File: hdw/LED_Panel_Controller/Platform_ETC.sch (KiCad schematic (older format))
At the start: 7 parts

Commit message: lots of schematic progress
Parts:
- U?: Configuration (none) -> ETC
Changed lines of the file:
@@
 encoding utf-8
 Sheet 14 34
-Title "Pulse Oximeter"
-Date "2020-08-01"
+Title "LED Panel Controller"
+Date "2020-12-23"
 Rev "A"
-Comp "Drew Maatman"
+Comp "Drew Maatman, Logan Wedel"
 Comment1 ""
 Comment2 ""
@@
 F 3 "https://datasheets.maximintegrated.com/en/ds/DS1683.pdf" H 4740 4400 60  0001 C CNN
 F 4 "DS1683S+-ND" H 4940 3850 60  0001 C CNN "Digi-Key PN"
+F 5 "ETC" H 4840 3640 50  0000 C CNN "Configuration"
 	1    4840 4100
 	1    0    0    -1

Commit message: made a lot more schematic progress
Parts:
- removed C? (x2): 10uF, Capacitors_SMD:C_0402, symbol Custom_Library:C_Custom
- added C? (x2): 10uF, Capacitors_SMD:C_0402, symbol Custom_Library:C_Custom
- C? (x2), D?: Configuration (none) -> ETC
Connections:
- net GND: now also C?.2, C?.2
- net at C?.1, C?.1, D?.1 (K)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: now also C?.1, C?.1
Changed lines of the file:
@@
 F 3 "www.st.com/resource/en/datasheet/bat48.pdf" H 2880 2660 50  0001 C CNN
 F 4 "497-5711-1-ND" H 2880 2660 50  0001 C CNN "Digi-Key PN"
+F 5 "ETC" V 2880 2830 50  0000 C CNN "Configuration"
 	1    2880 2660
 	0    -1   -1   0
@@
 F 6 "X5R" H 2730 3020 50  0000 R CNN "Dielectric"
 F 7 "490-13211-1-ND" H 2880 3120 50  0001 C CNN "Digi-Key PN"
+F 8 "ETC" H 2730 3300 50  0000 R CNN "Configuration"
 	1    2880 3120
-	1    0    0    -1
-$EndComp
-$Comp
-L Custom_Library:C_Custom C?
-U 1 1 5EC1781D
-P 3530 3120
-AR Path="/5CB7718D/5EC1781D" Ref="C?"  Part="1"
-AR Path="/5E0DC082/5EC1781D" Ref="C?"  Part="1"
-AR Path="/5E0F9110/5EC1781D" Ref="C?"  Part="1"
-AR Path="/5A557C58/5EC1781D" Ref="C?"  Part="1"
-AR Path="/5CB25152/5EC1781D" Ref="C?"  Part="1"
-AR Path="/5E697934/5EC1781D" Ref="C?"  Part="1"
-AR Path="/5EAE2F02/5EC1781D" Ref="C?"  Part="1"
-AR Path="/5EAE3021/5EC1781D" Ref="C?"  Part="1"
-AR Path="/5F582A92/5EC1781D" Ref="C?"  Part="1"
-F 0 "C?" H 3555 3220 50  0000 L CNN
-F 1 "10uF" H 3555 3020 50  0000 L CNN
-F 2 "Capacitors_SMD:C_0402" H 3568 2970 50  0001 C CNN
-F 3 "" H 3555 3220 50  0001 C CNN
-F 4 "0402" H 3380 3220 50  0000 R CNN "display_footprint"
-F 5 "6.3V" H 3380 3120 50  0000 R CNN "Voltage"
-F 6 "X5R" H 3380 3020 50  0000 R CNN "Dielectric"
-F 7 "490-13211-1-ND" H 3530 3120 50  0001 C CNN "Digi-Key PN"
-	1    3530 3120
-	1    0    0    -1
-$EndComp
-$Comp
-L Custom_Library:C_Custom C?
-U 1 1 5EC17E4D
-P 4180 3120
-AR Path="/5CB7718D/5EC17E4D" Ref="C?"  Part="1"
-AR Path="/5E0DC082/5EC17E4D" Ref="C?"  Part="1"
-AR Path="/5E0F9110/5EC17E4D" Ref="C?"  Part="1"
-AR Path="/5A557C58/5EC17E4D" Ref="C?"  Part="1"
-AR Path="/5CB25152/5EC17E4D" Ref="C?"  Part="1"
-AR Path="/5E697934/5EC17E4D" Ref="C?"  Part="1"
-AR Path="/5EAE2F02/5EC17E4D" Ref="C?"  Part="1"
-AR Path="/5EAE3021/5EC17E4D" Ref="C?"  Part="1"
-AR Path="/5F582A92/5EC17E4D" Ref="C?"  Part="1"
-F 0 "C?" H 4205 3220 50  0000 L CNN
-F 1 "10uF" H 4205 3020 50  0000 L CNN
-F 2 "Capacitors_SMD:C_0402" H 4218 2970 50  0001 C CNN
-F 3 "" H 4205 3220 50  0001 C CNN
-F 4 "0402" H 4030 3220 50  0000 R CNN "display_footprint"
-F 5 "6.3V" H 4030 3120 50  0000 R CNN "Voltage"
-F 6 "X5R" H 4030 3020 50  0000 R CNN "Dielectric"
-F 7 "490-13211-1-ND" H 4180 3120 50  0001 C CNN "Digi-Key PN"
-	1    4180 3120
 	1    0    0    -1
 $EndComp
@@
 F 6 "X7R" H 4680 3020 50  0000 R CNN "Dielectric"
 F 7 "490-10701-1-ND" H 5255 3620 60  0001 C CNN "Digi-Key PN"
+F 8 "ETC" H 4680 3300 50  0000 R CNN "Configuration"
 	1    4830 3120
 	1    0    0    -1
 $EndComp
+$Comp
+L Custom_Library:C_Custom C?
+U 1 1 601FEAD5
+P 3530 3120
+AR Path="/5CB7718D/601FEAD5" Ref="C?"  Part="1"
+AR Path="/5E0DC082/601FEAD5" Ref="C?"  Part="1"
+AR Path="/5E0F9110/601FEAD5" Ref="C?"  Part="1"
+AR Path="/5A557C58/601FEAD5" Ref="C?"  Part="1"
+AR Path="/5CB25152/601FEAD5" Ref="C?"  Part="1"
+AR Path="/5E697934/601FEAD5" Ref="C?"  Part="1"
+AR Path="/5EAE2F02/601FEAD5" Ref="C?"  Part="1"
+AR Path="/5EAE3021/601FEAD5" Ref="C?"  Part="1"
+AR Path="/5F582A92/601FEAD5" Ref="C?"  Part="1"
+F 0 "C?" H 3555 3220 50  0000 L CNN
+F 1 "10uF" H 3555 3020 50  0000 L CNN
+F 2 "Capacitors_SMD:C_0402" H 3568 2970 50  0001 C CNN
+F 3 "" H 3555 3220 50  0001 C CNN
+F 4 "0402" H 3380 3220 50  0000 R CNN "display_footprint"
+F 5 "6.3V" H 3380 3120 50  0000 R CNN "Voltage"
+F 6 "X5R" H 3380 3020 50  0000 R CNN "Dielectric"
+F 7 "490-13211-1-ND" H 3530 3120 50  0001 C CNN "Digi-Key PN"
+F 8 "ETC" H 3380 3300 50  0000 R CNN "Configuration"
+	1    3530 3120
+	1    0    0    -1
+$EndComp
+$Comp
+L Custom_Library:C_Custom C?
+U 1 1 601FEDDA
+P 4180 3120
+AR Path="/5CB7718D/601FEDDA" Ref="C?"  Part="1"
+AR Path="/5E0DC082/601FEDDA" Ref="C?"  Part="1"
+AR Path="/5E0F9110/601FEDDA" Ref="C?"  Part="1"
+AR Path="/5A557C58/601FEDDA" Ref="C?"  Part="1"
+AR Path="/5CB25152/601FEDDA" Ref="C?"  Part="1"
+AR Path="/5E697934/601FEDDA" Ref="C?"  Part="1"
+AR Path="/5EAE2F02/601FEDDA" Ref="C?"  Part="1"
+AR Path="/5EAE3021/601FEDDA" Ref="C?"  Part="1"
+AR Path="/5F582A92/601FEDDA" Ref="C?"  Part="1"
+F 0 "C?" H 4205 3220 50  0000 L CNN
+F 1 "10uF" H 4205 3020 50  0000 L CNN
+F 2 "Capacitors_SMD:C_0402" H 4218 2970 50  0001 C CNN
+F 3 "" H 4205 3220 50  0001 C CNN
+F 4 "0402" H 4030 3220 50  0000 R CNN "display_footprint"
+F 5 "6.3V" H 4030 3120 50  0000 R CNN "Voltage"
+F 6 "X5R" H 4030 3020 50  0000 R CNN "Dielectric"
+F 7 "490-13211-1-ND" H 4180 3120 50  0001 C CNN "Digi-Key PN"
+F 8 "ETC" H 4030 3300 50  0000 R CNN "Configuration"
+	1    4180 3120
+	1    0    0    -1
+$EndComp

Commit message: added digikey pns, footprints, bom scrubbed
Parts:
- C? (x3): Digi-Key PN 490-13211-1-ND -> 1276-1451-1-ND
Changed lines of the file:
@@
 F 5 "6.3V" H 2730 3120 50  0000 R CNN "Voltage"
 F 6 "X5R" H 2730 3020 50  0000 R CNN "Dielectric"
-F 7 "490-13211-1-ND" H 2880 3120 50  0001 C CNN "Digi-Key PN"
+F 7 "1276-1451-1-ND" H 2880 3120 50  0001 C CNN "Digi-Key PN"
 F 8 "ETC" H 2730 3300 50  0000 R CNN "Configuration"
 	1    2880 3120
@@
 F 5 "6.3V" H 3380 3120 50  0000 R CNN "Voltage"
 F 6 "X5R" H 3380 3020 50  0000 R CNN "Dielectric"
-F 7 "490-13211-1-ND" H 3530 3120 50  0001 C CNN "Digi-Key PN"
+F 7 "1276-1451-1-ND" H 3530 3120 50  0001 C CNN "Digi-Key PN"
 F 8 "ETC" H 3380 3300 50  0000 R CNN "Configuration"
 	1    3530 3120
@@
 F 5 "6.3V" H 4030 3120 50  0000 R CNN "Voltage"
 F 6 "X5R" H 4030 3020 50  0000 R CNN "Dielectric"
-F 7 "490-13211-1-ND" H 4180 3120 50  0001 C CNN "Digi-Key PN"
+F 7 "1276-1451-1-ND" H 4180 3120 50  0001 C CNN "Digi-Key PN"
 F 8 "ETC" H 4030 3300 50  0000 R CNN "Configuration"
 	1    4180 3120

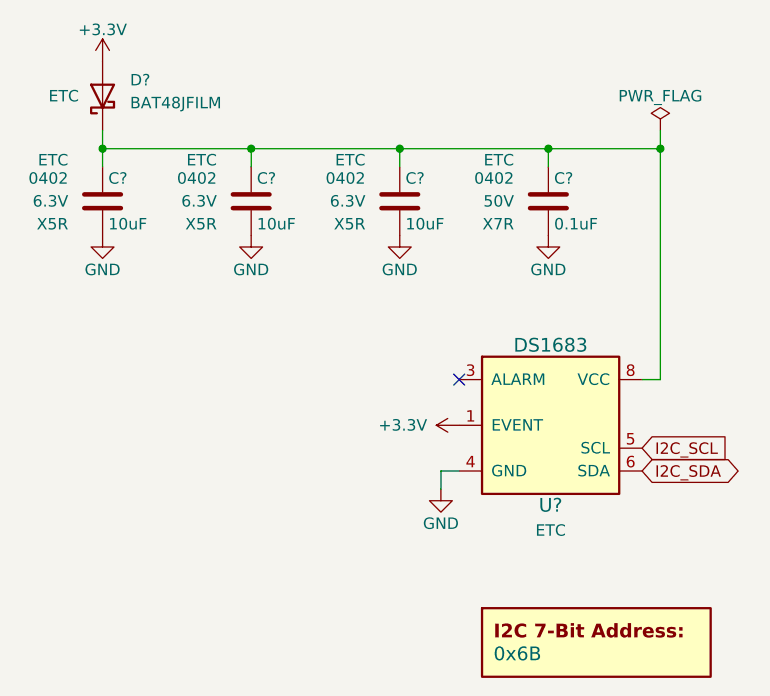
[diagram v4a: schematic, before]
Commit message: assigned I2C addresses
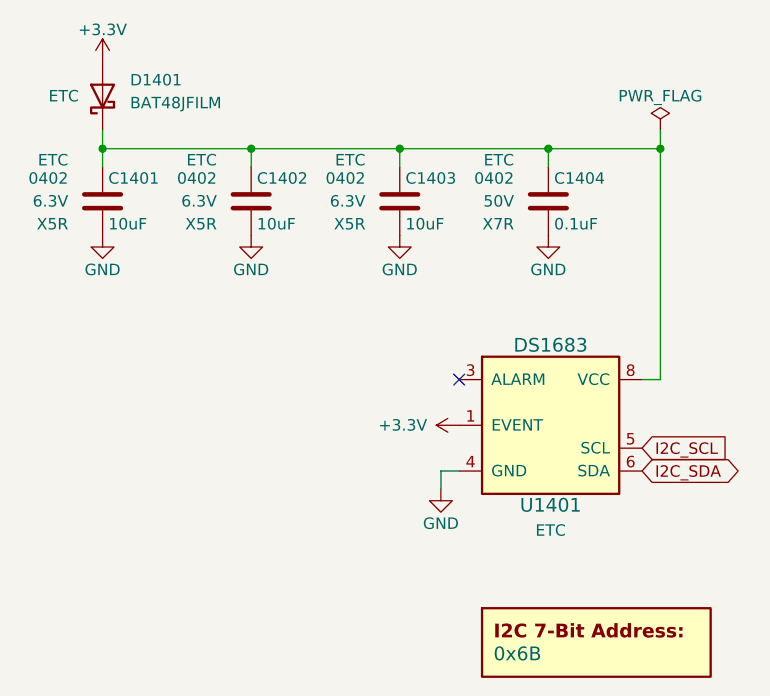
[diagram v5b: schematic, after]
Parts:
- gave numbers to parts that had none: 7
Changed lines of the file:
@@
 $EndDescr
 $Comp
-L Custom_Library:DS1683 U?
+L Custom_Library:DS1683 U1401
 U 1 1 5B5039F7
 P 4840 4100
-F 0 "U?" H 4840 3750 60  0000 C CNN
+F 0 "U1401" H 4840 3750 60  0000 C CNN
 F 1 "DS1683" H 4840 4450 60  0000 C CNN
 F 2 "Housings_SOIC:SOIC-8_3.9x4.9mm_Pitch1.27mm" H 4740 4400 60  0001 C CNN
@@
 NoConn ~ 4440 3900
 $Comp
-L power:GND #PWR?
+L power:GND #PWR01405
 U 1 1 5B50444E
 P 4360 4380
-F 0 "#PWR?" H 4360 4130 50  0001 C CNN
+F 0 "#PWR01405" H 4360 4130 50  0001 C CNN
 F 1 "GND" H 4360 4230 50  0000 C CNN
 F 2 "" H 4360 4380 50  0001 C CNN
@@
 	5320 3900 5240 3900
 $Comp
-L power:GND #PWR?
+L power:GND #PWR01407
 U 1 1 5B507BED
 P 4830 3270
-F 0 "#PWR?" H 4830 3020 50  0001 C CNN
+F 0 "#PWR01407" H 4830 3020 50  0001 C CNN
 F 1 "GND" H 4830 3120 50  0000 C CNN
 F 2 "" H 4830 3270 50  0001 C CNN
@@
 $EndComp
 $Comp
-L Custom_Library:I2C_Address DOC?
+L Custom_Library:I2C_Address DOC1401
 U 1 1 5E383387
 P 5040 5100
-F 0 "DOC?" H 5040 5350 60  0001 C CNN
+F 0 "DOC1401" H 5040 5350 60  0001 C CNN
 F 1 "0x6B" H 4590 5100 60  0000 L CNN
 F 2 "" H 5040 5450 60  0001 C CNN
@@
 $EndComp
 $Comp
-L power:GND #PWR?
+L power:GND #PWR01404
 U 1 1 5E2B2965
 P 4180 3270
-F 0 "#PWR?" H 4180 3020 50  0001 C CNN
+F 0 "#PWR01404" H 4180 3020 50  0001 C CNN
 F 1 "GND" H 4180 3120 50  0000 C CNN
 F 2 "" H 4180 3270 50  0001 C CNN
@@
 $EndComp
 $Comp
-L power:GND #PWR?
+L power:GND #PWR01403
 U 1 1 5E2B2CA6
 P 3530 3270
-F 0 "#PWR?" H 3530 3020 50  0001 C CNN
+F 0 "#PWR01403" H 3530 3020 50  0001 C CNN
 F 1 "GND" H 3530 3120 50  0000 C CNN
 F 2 "" H 3530 3270 50  0001 C CNN
@@
 $EndComp
 $Comp
-L power:GND #PWR?
+L power:GND #PWR01402
 U 1 1 5E2B305D
 P 2880 3270
-F 0 "#PWR?" H 2880 3020 50  0001 C CNN
+F 0 "#PWR01402" H 2880 3020 50  0001 C CNN
 F 1 "GND" H 2880 3120 50  0000 C CNN
 F 2 "" H 2880 3270 50  0001 C CNN
@@
 I2C_SDA
 $Comp
-L power:+3.3V #PWR?
+L power:+3.3V #PWR01406
 U 1 1 5E36CA22
 P 4440 4100
-F 0 "#PWR?" H 4440 3950 50  0001 C CNN
+F 0 "#PWR01406" H 4440 3950 50  0001 C CNN
 F 1 "+3.3V" V 4440 4240 50  0000 L CNN
 F 2 "" H 4440 4100 50  0001 C CNN
@@
 $EndComp
 $Comp
-L power:+3.3V #PWR?
+L power:+3.3V #PWR01401
 U 1 1 5E36D120
 P 2880 2510
-F 0 "#PWR?" H 2880 2360 50  0001 C CNN
+F 0 "#PWR01401" H 2880 2360 50  0001 C CNN
 F 1 "+3.3V" H 2880 2650 50  0000 C CNN
 F 2 "" H 2880 2510 50  0001 C CNN
@@
 $EndComp
 $Comp
-L power:PWR_FLAG #FLG?
+L power:PWR_FLAG #FLG01401
 U 1 1 5E4BADF7
 P 5320 2810
-F 0 "#FLG?" H 5320 2885 50  0001 C CNN
+F 0 "#FLG01401" H 5320 2885 50  0001 C CNN
 F 1 "PWR_FLAG" H 5320 2960 50  0000 C CNN
 F 2 "" H 5320 2810 50  0001 C CNN
@@
 AR Path="/5EAE2D8A/5EB6FFC8" Ref="D?"  Part="1"
 AR Path="/5EAE3021/5EB6FFC8" Ref="D?"  Part="1"
-AR Path="/5F582A92/5EB6FFC8" Ref="D?"  Part="1"
-F 0 "D?" V 2950 2540 50  0000 R CNN
+AR Path="/5F582A92/5EB6FFC8" Ref="D1401"  Part="1"
+F 0 "D1401" V 2950 2540 50  0000 R CNN
 F 1 "BAT48JFILM" V 2850 2540 50  0000 R CNN
 F 2 "Diode_SMD:D_SOD-323" H 2880 2485 50  0001 C CNN
@@
 AR Path="/5EAE2F02/5EC1774A" Ref="C?"  Part="1"
 AR Path="/5EAE3021/5EC1774A" Ref="C?"  Part="1"
-AR Path="/5F582A92/5EC1774A" Ref="C?"  Part="1"
-F 0 "C?" H 2905 3220 50  0000 L CNN
+AR Path="/5F582A92/5EC1774A" Ref="C1401"  Part="1"
+F 0 "C1401" H 2905 3220 50  0000 L CNN
 F 1 "10uF" H 2905 3020 50  0000 L CNN
 F 2 "Capacitors_SMD:C_0402" H 2918 2970 50  0001 C CNN
@@
 AR Path="/5EAE2D66/5EC1A081" Ref="C?"  Part="1"
 AR Path="/5EAE3021/5EC1A081" Ref="C?"  Part="1"
-AR Path="/5F582A92/5EC1A081" Ref="C?"  Part="1"
-F 0 "C?" H 4855 3220 50  0000 L CNN
+AR Path="/5F582A92/5EC1A081" Ref="C1404"  Part="1"
+F 0 "C1404" H 4855 3220 50  0000 L CNN
 F 1 "0.1uF" H 4855 3020 50  0000 L CNN
 F 2 "Capacitors_SMD:C_0402" H 4868 2970 50  0001 C CNN
@@
 AR Path="/5EAE2F02/601FEAD5" Ref="C?"  Part="1"
 AR Path="/5EAE3021/601FEAD5" Ref="C?"  Part="1"
-AR Path="/5F582A92/601FEAD5" Ref="C?"  Part="1"
-F 0 "C?" H 3555 3220 50  0000 L CNN
+AR Path="/5F582A92/601FEAD5" Ref="C1402"  Part="1"
+F 0 "C1402" H 3555 3220 50  0000 L CNN
 F 1 "10uF" H 3555 3020 50  0000 L CNN
 F 2 "Capacitors_SMD:C_0402" H 3568 2970 50  0001 C CNN
@@
 AR Path="/5EAE2F02/601FEDDA" Ref="C?"  Part="1"
 AR Path="/5EAE3021/601FEDDA" Ref="C?"  Part="1"
-AR Path="/5F582A92/601FEDDA" Ref="C?"  Part="1"
-F 0 "C?" H 4205 3220 50  0000 L CNN
+AR Path="/5F582A92/601FEDDA" Ref="C1403"  Part="1"
+F 0 "C1403" H 4205 3220 50  0000 L CNN
 F 1 "10uF" H 4205 3020 50  0000 L CNN
 F 2 "Capacitors_SMD:C_0402" H 4218 2970 50  0001 C CNN

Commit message: added BOMs, some consolidation
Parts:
- C1404: Digi-Key PN 490-10701-1-ND -> 490-10698-1-ND
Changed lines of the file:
@@
 F 5 "50V" H 4680 3120 50  0000 R CNN "Voltage"
 F 6 "X7R" H 4680 3020 50  0000 R CNN "Dielectric"
-F 7 "490-10701-1-ND" H 5255 3620 60  0001 C CNN "Digi-Key PN"
+F 7 "490-10698-1-ND" H 5255 3620 60  0001 C CNN "Digi-Key PN"
 F 8 "ETC" H 4680 3300 50  0000 R CNN "Configuration"
 	1    4830 3120
